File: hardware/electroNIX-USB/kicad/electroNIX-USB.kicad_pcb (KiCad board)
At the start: 2 copper layers, 102 x 66 mm, 129 parts, among them J1 USB-C (USB 2.0), Q1 MMBT3904, Q10 MMBTA42, Q11 MMBTA92, Q12 MMBTA42, Q13 MMBTA42, Q14 MMBTA42, Q15 MMBTA42, Q16 MMBTA42, Q17 MMBTA42, Q18 MMBTA42, Q19 MMBTA42, Q2 MMBT3904, Q20 MMBTA42, Q21 MMBTA42, Q22 MMBTA42, Q23 MMBTA42, Q3 IRLR3110ZPBF, Q4 MMBTA42, Q5 MMBTA92, Q6 MMBTA42, Q7 MMBTA92, Q8 MMBTA42, Q9 MMBTA92, SW1 RESET, SW2 BOOT, SW3 SET, U1 USBLC6-2SC6, U2 AMS1117-3.3, U3 CH340C, U4 ESP32-WROOM-32E-N4

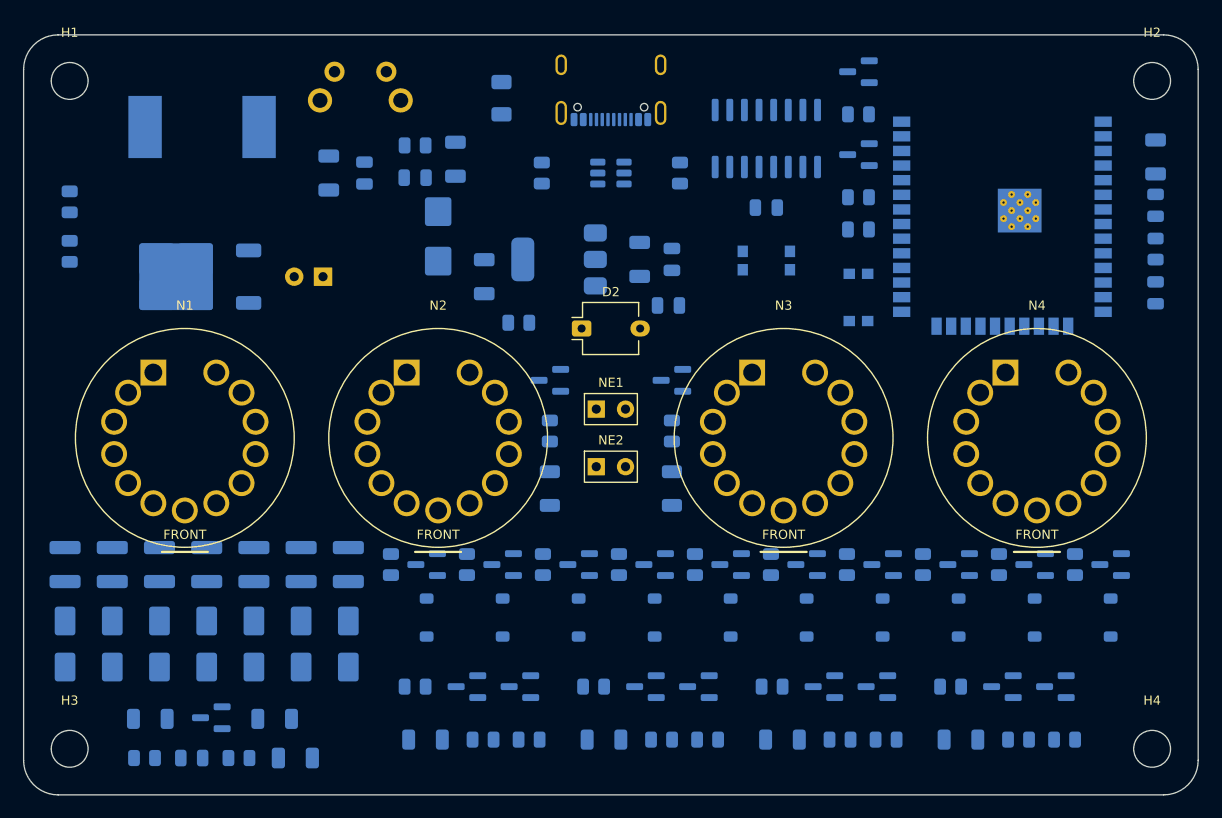
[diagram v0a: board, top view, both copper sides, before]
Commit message: electroNIX-USB: drop all switches, regroup board placement by circuit
- No RESET/BOOT/SET: the firmware reads no button, and the CH340C
  DTR/RTS auto-reset handles flashing. SET's pull-up and cap are gone.
- Boost converter is a compact loop (input caps -> L1 -> FET tab) feeding
  the multiplier columns in chain order.
- ESP32: 3V3 decoupling at pin 2, EN RC at pin 3, HV feedback divider and
  clamp at IO35; auto-reset between the CH340C and the module's UART pins.
- Front band spread out: output cap + KBIAS left, cathode row, one anode
  cluster under each tube.
- 6-tube board placed too (150 x 66 mm). Both boards unrouted.

Co-Authored-By: Claude Opus 5.5 <noreply@anthropic.com>
Claude-Session: https://claude.ai/code/session_01AFMfevKEKDGbci8uJGhf4W
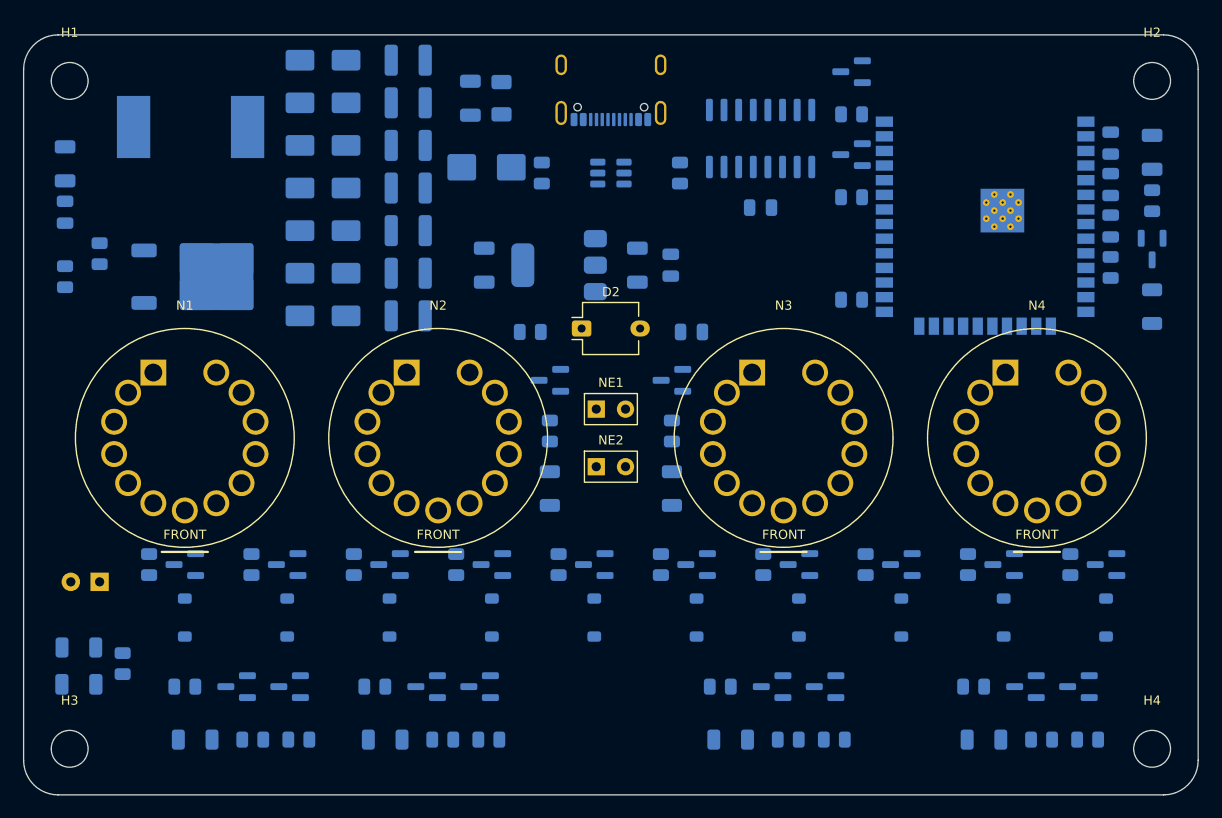
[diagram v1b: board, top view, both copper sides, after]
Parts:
- removed C22: 2u2 50V, C_1206_3216Metric
- removed R44: 100k, R_0805_2012Metric
- removed SW1: RESET, SW_Push_1P1T_NO_CK_KMR2
- removed SW2: BOOT, SW_Push_1P1T_NO_CK_KMR2
- removed SW3: SET, SW_Tactile_SPST_Angled_PTS645Vx31-2LFS
- C10: value 100n -> 22u 10V; footprint C_0805_2012Metric -> C_1206_3216Metric
- C11: value 22u 10V -> 100n; footprint C_1206_3216Metric -> C_0805_2012Metric
- C12: value 100n -> 2u2 100V; footprint C_0805_2012Metric -> C_1210_3225Metric
- C19: value 2u2 100V -> 2u2 250V; footprint C_1210_3225Metric -> CP_Radial_D6.3mm_P2.50mm
- C20: value 2u2 250V -> 100n; footprint CP_Radial_D6.3mm_P2.50mm -> C_0805_2012Metric
- C21: value 100n -> 2u2 50V; footprint C_0805_2012Metric -> C_1206_3216Metric
- R10: value 10k -> 430k; footprint R_0805_2012Metric -> R_1206_3216Metric
- R11: value 430k -> 6k2; footprint R_1206_3216Metric -> R_0805_2012Metric
- R12: value 6k2 -> 15k
- R13, R17, R21, R25: value 15k -> 430k; footprint R_0805_2012Metric -> R_1206_3216Metric
- R14, R18, R22, R26, R43: value 430k -> 100k; footprint R_1206_3216Metric -> R_0805_2012Metric
- R15, R19, R23, R27: value 100k -> 5k6
- R16, R20, R24: value 5k6 -> 15k
- R28: value 5k6 -> 6k8
- R38: value 6k8 -> 47k
- R39, R41: value 47k -> 150k; footprint R_0805_2012Metric -> R_1206_3216Metric
- R40: value 150k -> 47k; footprint R_1206_3216Metric -> R_0805_2012Metric
- R42: value 150k -> 430k
- R8: value 10k -> 10R
- R9: value 10R -> 10k
- moved R10 94.1 mm to (198.0, 123.6)
- moved R11 92.2 mm to (194.4, 120.2), turned to -90 degrees
- moved D10 91.3 mm to (198.0, 118.6), turned to -90 degrees
- moved R28 80.9 mm to (110.9, 146.0), turned to -90 degrees
- moved C20 68.5 mm to (194.4, 116.6), turned to -90 degrees
- moved R42 53.3 mm to (104.8, 153.2), turned to 180 degrees
- moved D9 50.7 mm to (126.0, 102.2), turned to 180 degrees
- moved C14 47.6 mm to (133.4, 105.9), turned to 180 degrees
- moved R38 47.1 mm to (145.7, 134.4)
- moved D8 47.0 mm to (126.0, 105.9), turned to 180 degrees
- moved C18 44.8 mm to (133.4, 102.2), turned to 180 degrees
- moved D7 43.7 mm to (126.0, 109.6), turned to 180 degrees
- moved C15 42.3 mm to (133.4, 109.6), turned to 180 degrees
- moved C13 41.6 mm to (133.4, 117.0), turned to 180 degrees
- moved D6 40.9 mm to (126.0, 113.3), turned to 180 degrees
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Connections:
- C10 pad 1: /ESP32/BTN -> +5V
- C12 pad 1: +5V -> +170V
- C12 pad 2: GND -> /HV supply/CW_T3
- C13 pad 1: +170V -> /HV supply/CW_T3
- C13 pad 2: /HV supply/CW_T3 -> /HV supply/CW_T2
- C14 pad 1: /HV supply/CW_T3 -> /HV supply/CW_T2
- C14 pad 2: /HV supply/CW_T2 -> /HV supply/CW_T1
- C15 pad 1: /HV supply/CW_T2 -> /HV supply/CW_T1
- C15 pad 2: /HV supply/CW_T1 -> GND
- C16 pad 1: /HV supply/CW_T1 -> /HV supply/CW_B3
- C16 pad 2: GND -> /HV supply/CW_B2
- C17 pad 1: /HV supply/CW_B3 -> /HV supply/CW_B2
- C17 pad 2: /HV supply/CW_B2 -> /HV supply/CW_B1
- C18 pad 1: /HV supply/CW_B2 -> /HV supply/CW_B1
- C18 pad 2: /HV supply/CW_B1 -> /HV supply/HV_SW
- C19 pad 1: /HV supply/CW_B1 -> +170V
- C19 pad 2: /HV supply/HV_SW -> GND
- C20 pad 1: +170V -> KOMP_170V
- C21 pad 1: KOMP_170V -> /Display/KBIAS
- R10 pad 1: PWM -> +170V
- R10 pad 2: GND -> KOMP_170V
- R11 pad 1: +170V -> KOMP_170V
- R11 pad 2: KOMP_170V -> GND
- R12 pad 1: KOMP_170V -> W_1
- R12 pad 2: GND -> Net-(Q4-B)
- R13 pad 1: W_1 -> Net-(Q5-B)
- R13 pad 2: Net-(Q4-B) -> Net-(Q4-C)
- R14 pad 1: Net-(Q5-B) -> +170V
- R14 pad 2: Net-(Q4-C) -> Net-(Q5-B)
- R15 pad 1: +170V -> Net-(Q5-C)
- R15 pad 2: Net-(Q5-B) -> /Display/A_1
- R16 pad 1: Net-(Q5-C) -> W_2
- R16 pad 2: /Display/A_1 -> Net-(Q6-B)
- R17 pad 1: W_2 -> Net-(Q7-B)
- R17 pad 2: Net-(Q6-B) -> Net-(Q6-C)
- R18 pad 1: Net-(Q7-B) -> +170V
- R18 pad 2: Net-(Q6-C) -> Net-(Q7-B)
- R19 pad 1: +170V -> Net-(Q7-C)
- R19 pad 2: Net-(Q7-B) -> /Display/A_2
- R20 pad 1: Net-(Q7-C) -> W_3
- R20 pad 2: /Display/A_2 -> Net-(Q8-B)
- R21 pad 1: W_3 -> Net-(Q9-B)
- R21 pad 2: Net-(Q8-B) -> Net-(Q8-C)
- R22 pad 1: Net-(Q9-B) -> +170V
- R22 pad 2: Net-(Q8-C) -> Net-(Q9-B)
- R23 pad 1: +170V -> Net-(Q9-C)
- R23 pad 2: Net-(Q9-B) -> /Display/A_3
- R24 pad 1: Net-(Q9-C) -> W_4
- R24 pad 2: /Display/A_3 -> Net-(Q10-B)
- R25 pad 1: W_4 -> Net-(Q11-B)
- R25 pad 2: Net-(Q10-B) -> Net-(Q10-C)
- R26 pad 1: Net-(Q11-B) -> +170V
- R26 pad 2: Net-(Q10-C) -> Net-(Q11-B)
- R27 pad 1: +170V -> Net-(Q11-C)
- R27 pad 2: Net-(Q11-B) -> /Display/A_4
- R28 pad 1: Net-(Q11-C) -> C_0
- R28 pad 2: /Display/A_4 -> Net-(Q12-B)
- R29 pad 1: C_0 -> C_1
- R29 pad 2: Net-(Q12-B) -> Net-(Q13-B)
- R30 pad 1: C_1 -> C_2
- R30 pad 2: Net-(Q13-B) -> Net-(Q14-B)
- R31 pad 1: C_2 -> C_3
- R31 pad 2: Net-(Q14-B) -> Net-(Q15-B)
- R32 pad 1: C_3 -> C_4
- R32 pad 2: Net-(Q15-B) -> Net-(Q16-B)
- R33 pad 1: C_4 -> C_5
- R33 pad 2: Net-(Q16-B) -> Net-(Q17-B)
- R34 pad 1: C_5 -> C_6
- R34 pad 2: Net-(Q17-B) -> Net-(Q18-B)
- R35 pad 1: C_6 -> C_7
- R35 pad 2: Net-(Q18-B) -> Net-(Q19-B)
- R36 pad 1: C_7 -> C_8
- R36 pad 2: Net-(Q19-B) -> Net-(Q20-B)
- R37 pad 1: C_8 -> C_9
- R37 pad 2: Net-(Q20-B) -> Net-(Q21-B)
- R38 pad 1: C_9 -> SEC_0
- R38 pad 2: Net-(Q21-B) -> Net-(Q22-B)
- R39 pad 1: SEC_0 -> +170V
- R39 pad 2: Net-(Q22-B) -> Net-(NE1-Pad2)
- R40 pad 1: +170V -> SEC_1
- R40 pad 2: Net-(NE1-Pad2) -> Net-(Q23-B)
- R41 pad 1: SEC_1 -> +170V
- R41 pad 2: Net-(Q23-B) -> Net-(NE2-Pad2)
- R42 pad 2: Net-(NE2-Pad2) -> /Display/KBIAS
- R43 pad 1: +170V -> /Display/KBIAS
- R43 pad 2: /Display/KBIAS -> GND
- R8 pad 1: +3V3 -> PWM
- R8 pad 2: /ESP32/BTN -> Net-(Q3-G)
- R9 pad 2: Net-(Q3-G) -> GND
- U4 pad 4: /ESP32/BTN -> (no net)

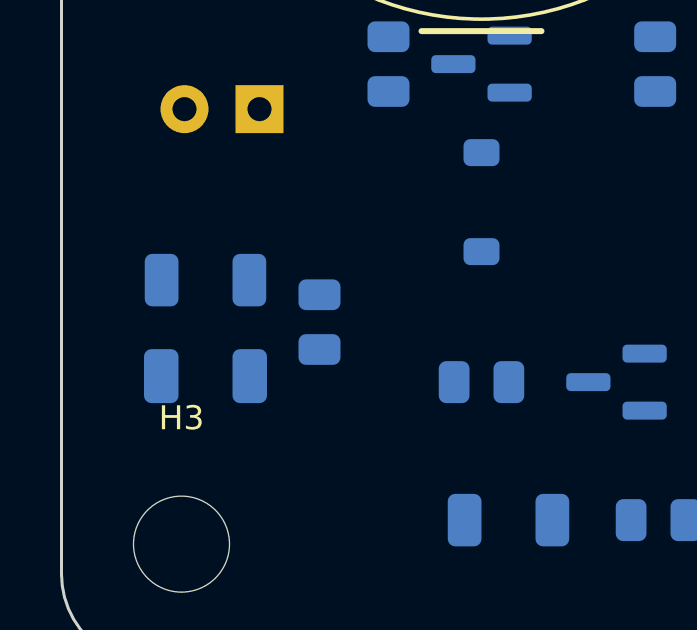
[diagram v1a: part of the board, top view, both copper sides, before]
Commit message: electroNIX-USB: restore PCB-036 KBIAS capacitor string (4 x 470n in series)
C41-C44 on PCB-036 are in series (118 nF, 200 V string) across R46, not
in parallel. Replace the single 2.2 uF/50 V cap with the original series
string and place it beside the 430k/100k divider.

Co-Authored-By: Claude Opus 5.5 <noreply@anthropic.com>
Claude-Session: https://claude.ai/code/session_01AFMfevKEKDGbci8uJGhf4W
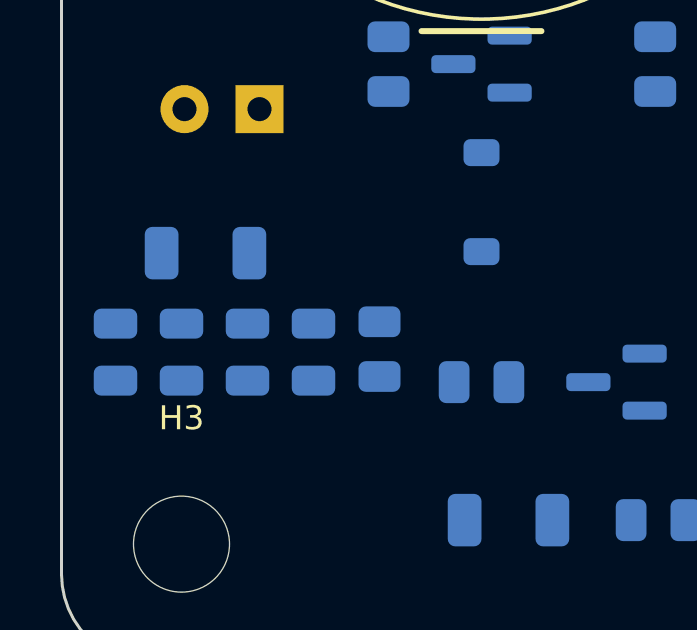
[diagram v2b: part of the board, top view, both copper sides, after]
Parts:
- added C22: 470n 50V, C_0805_2012Metric, B.Cu at (104.0, 155.6)
- added C23: 470n 50V, C_0805_2012Metric, B.Cu at (106.2, 155.6)
- added C24: 470n 50V, C_0805_2012Metric, B.Cu at (108.4, 155.6)
- C21: value 2u2 50V -> 470n 50V; footprint C_1206_3216Metric -> C_0805_2012Metric
- moved C21 3.10 mm to (101.8, 155.6), turned to -90 degrees
- moved R43 2.19 mm to (110.6, 155.5)
- moved R42 0.90 mm to (104.8, 152.3)
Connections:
- C21 pad 2: GND -> Net-(C21-Pad2)

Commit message: electroNIX-USB: boost gate pull-down gate-to-source as on PCB-036
R45 on PCB-036 pulls the FET gate (after the 10R) to GND; ours sat on
the IO2 side. Move it to the gate and place it at the gate pad. Add a
note listing what was checked against the PCB-036 schematic.

Co-Authored-By: Claude Opus 5.5 <noreply@anthropic.com>
Claude-Session: https://claude.ai/code/session_01AFMfevKEKDGbci8uJGhf4W
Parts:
- moved R9 3.97 mm to (106.6, 123.6)
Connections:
- R9 pad 1: PWM -> Net-(Q3-G)

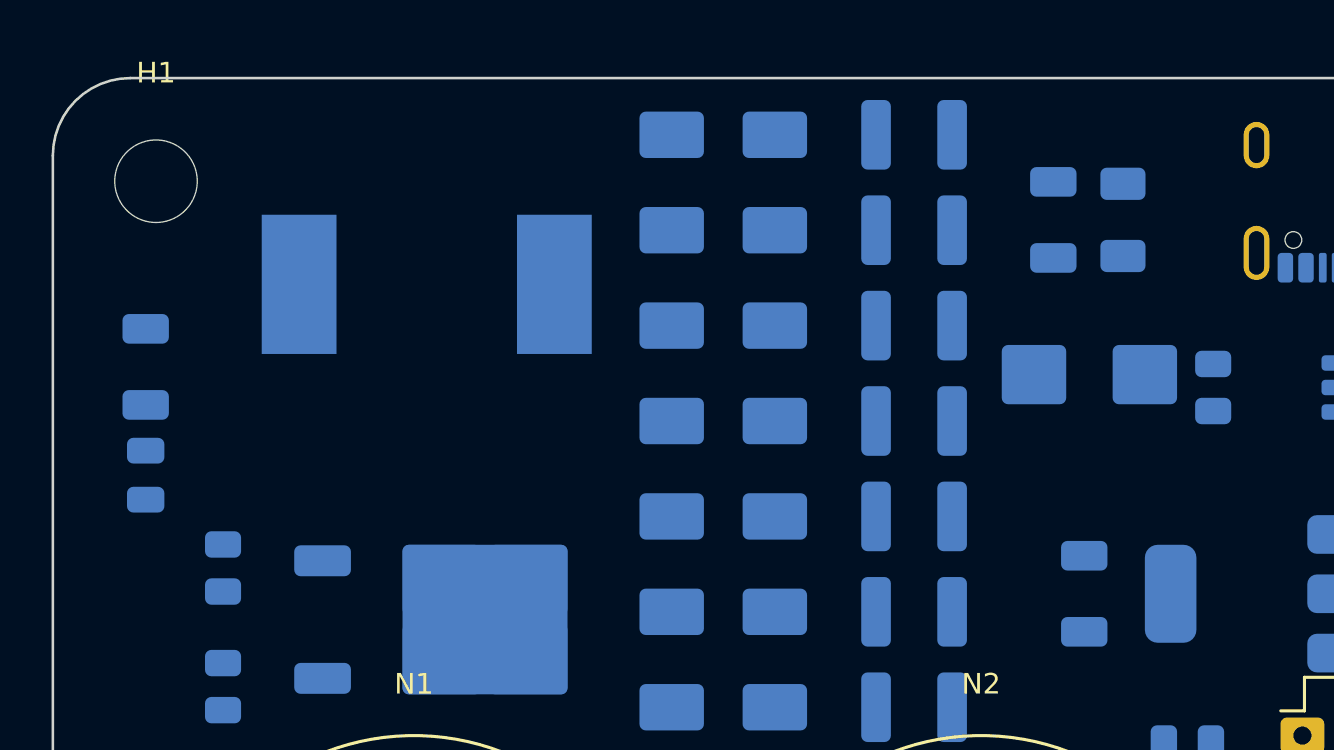
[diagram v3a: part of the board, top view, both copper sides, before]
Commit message: electroNIX-USB: tantalum bulk caps on the 5 V input and boost input
Back to PCB-036's 22 uF/35 V tantalum (7343 D case) for the boost input
and use the same part for the USB-C bulk cap. It holds its value at 5 V,
unlike a small MLCC, and its ESR damps hot-plug ringing on the cable.
The 100 nF ceramics stay. Placement adjusted around the larger parts.

Co-Authored-By: Claude Opus 5.5 <noreply@anthropic.com>
Claude-Session: https://claude.ai/code/session_01AFMfevKEKDGbci8uJGhf4W
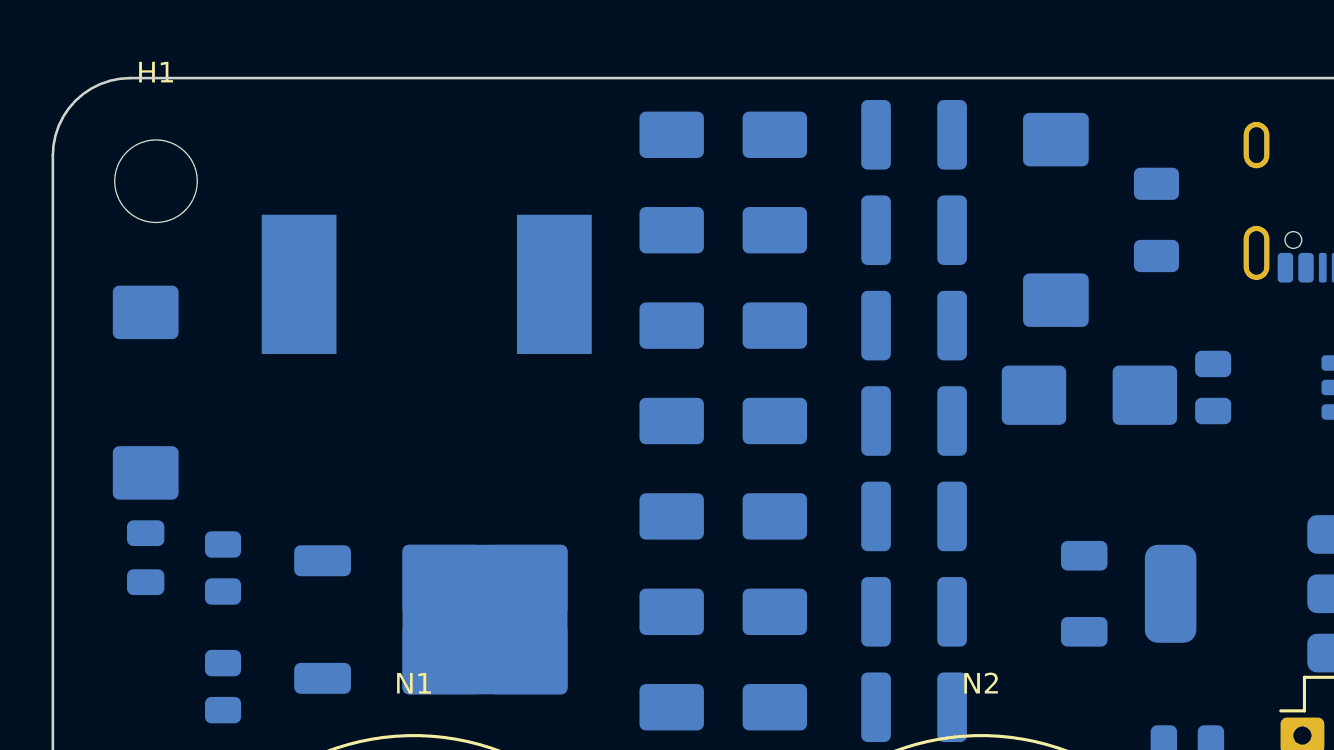
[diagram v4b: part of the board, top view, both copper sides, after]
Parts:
- C1, C10: value 22u 10V -> 22u 35V tant.; footprint C_1206_3216Metric -> CP_EIA-7343-31_Kemet-D
- moved C11 3.20 mm to (103.6, 118.6)
- moved F1 1.30 mm to (142.8, 105.5)
- moved C10 1.00 mm to (103.6, 112.2)
- moved D1 0.80 mm to (140.2, 112.3)
- moved C1 0.10 mm to (138.9, 105.5)

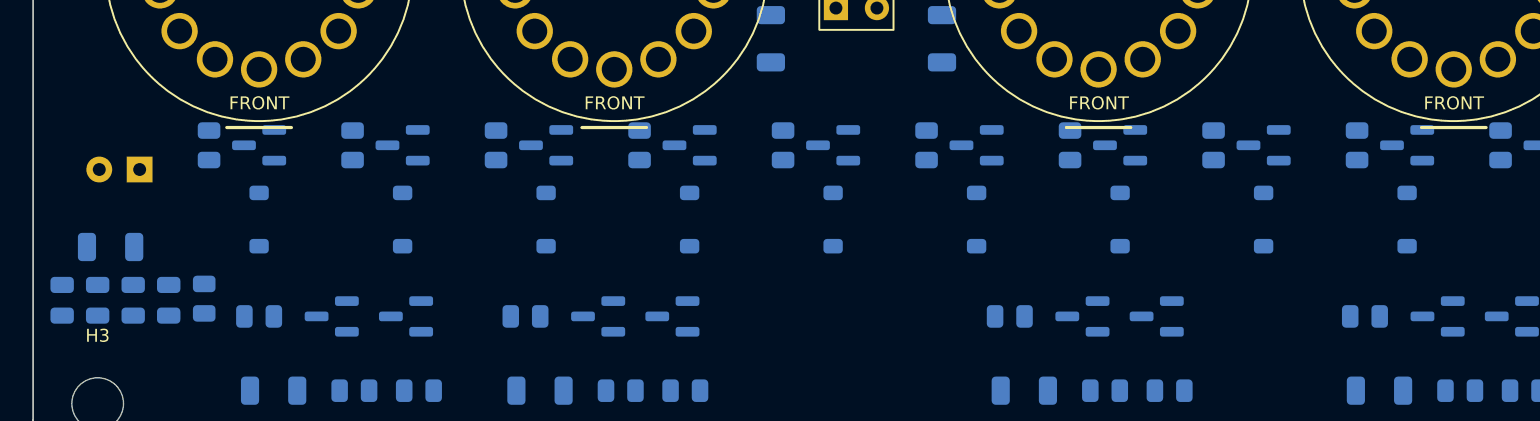
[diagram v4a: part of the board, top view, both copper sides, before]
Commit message: electroNIX-USB: lay the 170 V output electrolytic flat
New footprint CP_Radial_D8mm_P2.50mm_Lying (2.5 mm leads, keep-clear for
a body up to 8 x 12.5 mm folded flat). C19 now runs along the left edge
toward the front; KBIAS parts and the cathode row moved right to clear it.

Co-Authored-By: Claude Opus 5.5 <noreply@anthropic.com>
Claude-Session: https://claude.ai/code/session_01AFMfevKEKDGbci8uJGhf4W
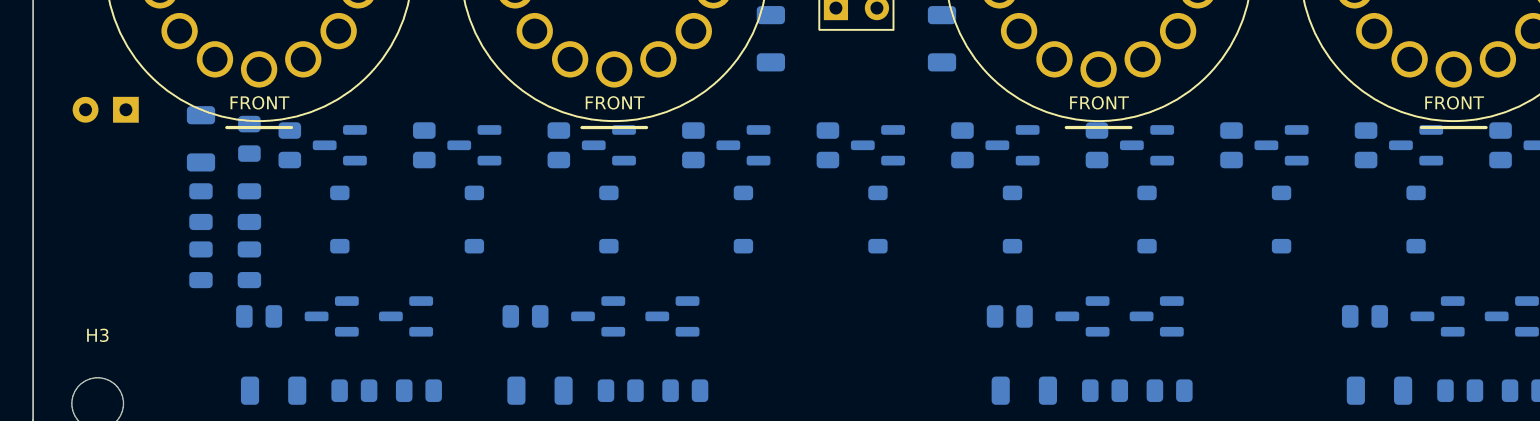
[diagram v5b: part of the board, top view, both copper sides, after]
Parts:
- C19: footprint CP_Radial_D6.3mm_P2.50mm -> CP_Radial_D8mm_P2.50mm_Lying
- moved C22 11.0 mm to (113.4, 149.8)
- moved C21 10.4 mm to (110.4, 149.8)
- moved R43 10.3 mm to (113.4, 145.6)
- moved R42 8.73 mm to (110.4, 145.6), turned to -90 degrees
- moved C24 5.46 mm to (113.4, 153.4)
- moved D11 5.00 mm to (119.0, 150.6)
- moved Q12 5.00 mm to (119.0, 146.0)
- moved R28 5.00 mm to (115.9, 146.0)
- moved C23 4.74 mm to (110.4, 153.4)
- moved D12 4.44 mm to (127.3, 150.6)
- moved Q13 4.44 mm to (127.3, 146.0)
- moved R29 4.44 mm to (124.2, 146.0)
- moved D13 3.89 mm to (135.7, 150.6)
- moved Q14 3.89 mm to (135.7, 146.0)
- moved R30 3.89 mm to (132.6, 146.0)
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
